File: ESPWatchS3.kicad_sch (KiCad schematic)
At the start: 137 parts, among them J1 USB, J2 OLED, J3 UART0, Q1 DMN2050LFDB, SW1 Reset, SW2 Boot, SW3 User 1, SW4 User 2, SW5 User 3, SW6 User 4, U1 ESP32-S3R8, U10 BD48KxxG, U11 NJG1143UA2-TE1, U2 EVA-M8Q-0, U3 BME280, U4 TPS631000DRLR, U5 AP3012, U6 BQ298012, U7 BQ27441-G1A, U8 BQ24075RGTR, U9 IS25LP128F-JKLE, Y1 40MHz, Y2 32.768kHz, Y3 32.768kHz

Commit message: PCB Work
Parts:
- removed C4: 0.1u, Capacitor_SMD:C_0402_1005Metric, symbol Device:C_Small
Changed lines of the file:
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@@
     (stroke (width 0) (type default))
   )
-  (wire (pts (xy 33.655 106.045) (xy 33.655 108.585))
-    (stroke (width 0) (type default))
-  )
   (wire (pts (xy 51.435 61.595) (xy 51.435 60.325))
     (stroke (width 0) (type default))
@@
     (stroke (width 0) (type default))
   )
-  (wire (pts (xy 26.035 98.425) (xy 33.655 98.425))
-    (stroke (width 0) (type default))
-  )
   (wire (pts (xy 132.715 47.625) (xy 142.24 47.625))
     (stroke (width 0) (type default))
@@
     (stroke (width 0) (type default))
   )
-  (wire (pts (xy 33.655 98.425) (xy 33.655 100.965))
-    (stroke (width 0) (type default))
-  )
   (wire (pts (xy 158.75 186.055) (xy 156.21 186.055))
     (stroke (width 0) (type default))
@@
     )
   )
-  (symbol (lib_id "Device:C_Small") (at 33.655 103.505 0) (unit 1)
-    (in_bom yes) (on_board yes) (dnp no)
-    (property "Reference" "C4" (at 33.655 101.6 0)
-      (effects (font (size 1.27 1.27)) (justify left))
-    )
-    (property "Value" "0.1u" (at 33.655 106.045 0)
-      (effects (font (size 1.27 1.27)) (justify left))
-    )
-    (property "Footprint" "Capacitor_SMD:C_0402_1005Metric" (at 33.655 103.505 0)
-      (effects (font (size 1.27 1.27)) hide)
-    )
-    (property "Datasheet" "~" (at 33.655 103.505 0)
-      (effects (font (size 1.27 1.27)) hide)
-    )
-    (pin "1")
-    (pin "2")
-    (instances
-      (project "ESPWatchS3"
-        (path "/bf5b2c41-bb33-4360-ba29-22d569e03292"
-          (reference "C4") (unit 1)
-        )
-      )
-    )
-  )
   (symbol (lib_id "power:GND") (at 104.775 159.385 0) (unit 1)
     (in_bom yes) (on_board yes) (dnp no) (fields_autoplaced)
@@
         )
       )
-    )
-  )
-  (symbol (lib_id "power:GND") (at 33.655 108.585 0) (unit 1)
-    (in_bom yes) (on_board yes) (dnp no) (fields_autoplaced)
-    (property "Reference" "#PWR024" (at 33.655 114.935 0)
-      (effects (font (size 1.27 1.27)) hide)
-    )
-    (property "Value" "GND" (at 33.655 113.665 0)
-      (effects (font (size 1.27 1.27)))
-    )
-    (property "Footprint" "" (at 33.655 108.585 0)
-      (effects (font (size 1.27 1.27)) hide)
-    )
-    (property "Datasheet" "" (at 33.655 108.585 0)
-      (effects (font (size 1.27 1.27)) hide)
-    )
-    (pin "1")
-    (instances
-      (project "ESPWatchS3"
-        (path "/bf5b2c41-bb33-4360-ba29-22d569e03292"
-          (reference "#PWR024") (unit 1)
-        )
-      )

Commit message: More changes
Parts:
- removed C27: 1u, Capacitor_SMD:C_0603_1608Metric, symbol Device:C_Small
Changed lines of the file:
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@@
   (junction (at 186.69 29.845) (diameter 0) (color 0 0 0 0)
   )
-  (junction (at 368.935 95.25) (diameter 0) (color 0 0 0 0)
-  )
   (junction (at 132.08 186.69) (diameter 0) (color 0 0 0 0)
   )
@@
     (stroke (width 0) (type default))
   )
-  (wire (pts (xy 368.935 104.775) (xy 368.935 113.03))
-    (stroke (width 0) (type default))
-  )
   (wire (pts (xy 34.29 215.265) (xy 29.845 215.265))
     (stroke (width 0) (type default))
@@
     (stroke (width 0) (type default))
   )
-  (wire (pts (xy 368.935 99.695) (xy 368.935 95.25))
-    (stroke (width 0) (type default))
-  )
   (wire (pts (xy 225.425 127.635) (xy 229.87 127.635))
     (stroke (width 0) (type default))
@@
     )
   )
-  (symbol (lib_id "power:GND") (at 368.935 113.03 0) (unit 1)
-    (in_bom yes) (on_board yes) (dnp no) (fields_autoplaced)
-    (property "Reference" "#PWR080" (at 368.935 119.38 0)
-      (effects (font (size 1.27 1.27)) hide)
-    )
-    (property "Value" "GND" (at 368.935 118.11 0)
-      (effects (font (size 1.27 1.27)))
-    )
-    (property "Footprint" "" (at 368.935 113.03 0)
-      (effects (font (size 1.27 1.27)) hide)
-    )
-    (property "Datasheet" "" (at 368.935 113.03 0)
-      (effects (font (size 1.27 1.27)) hide)
-    )
-    (pin "1")
-    (instances
-      (project "ESPWatchS3"
-        (path "/bf5b2c41-bb33-4360-ba29-22d569e03292"
-          (reference "#PWR080") (unit 1)
-        )
-      )
-    )
-  )
   (symbol (lib_id "Device:C_Small") (at 39.37 36.195 0) (unit 1)
     (in_bom yes) (on_board yes) (dnp no) (fields_autoplaced)
@@
         )
       )
-    )
-  )
-  (symbol (lib_id "Device:C_Small") (at 368.935 102.235 0) (mirror y) (unit 1)
-    (in_bom yes) (on_board yes) (dnp no)
-    (property "Reference" "C27" (at 374.015 100.33 0)
-      (effects (font (size 1.27 1.27)) (justify left))
-    )
-    (property "Value" "1u" (at 374.015 102.235 0)
-      (effects (font (size 1.27 1.27)) (justify left))
-    )
-    (property "Footprint" "Capacitor_SMD:C_0603_1608Metric" (at 368.935 102.235 0)
-      (effects (font (size 1.27 1.27)) hide)
-    )
-    (property "Datasheet" "~" (at 368.935 102.235 0)
-      (effects (font (size 1.27 1.27)) hide)
-    )
-    (pin "1")
-    (pin "2")
-    (instances
-      (project "ESPWatchS3"
-        (path "/bf5b2c41-bb33-4360-ba29-22d569e03292"
-          (reference "C27") (unit 1)
-        )
-      )

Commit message: More PCB Work
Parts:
- removed C11, C15, C16: 0.1u, Capacitor_SMD:C_0402_1005Metric, symbol Device:C_Small
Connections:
- net OLED_RES is gone; now on net OLED_RST: J2.11 (Pin_11)

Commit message: More PCB work
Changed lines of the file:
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@@
-    (stroke (width 0) (type default))
-  )
-  (wire (pts (xy 132.08 197.485) (xy 132.08 186.69))
     (stroke (width 0) (type default))
   )
@@
     (stroke (width 0) (type default))
   )
+  (wire (pts (xy 132.08 186.69) (xy 132.08 197.485))
+    (stroke (width 0) (type default))
+  )

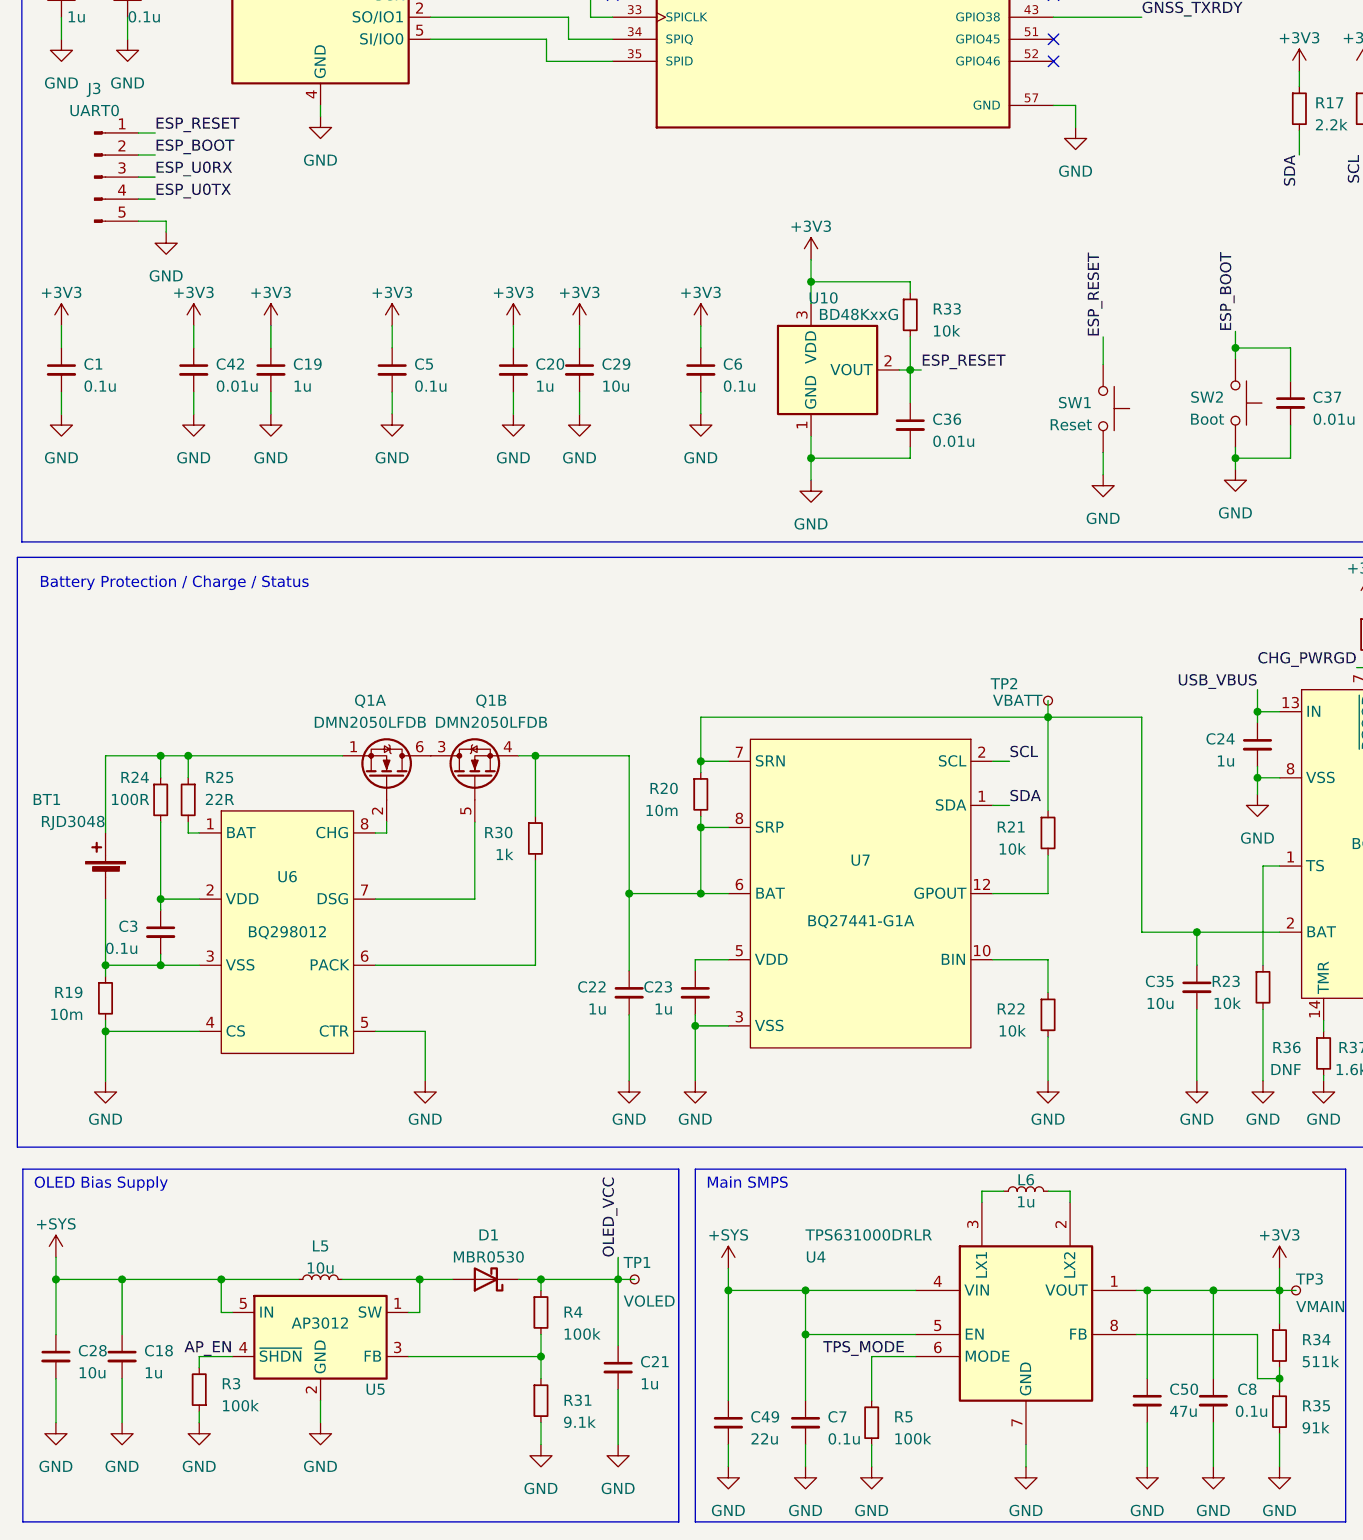
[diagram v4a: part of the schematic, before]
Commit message: Almost done PCB routing
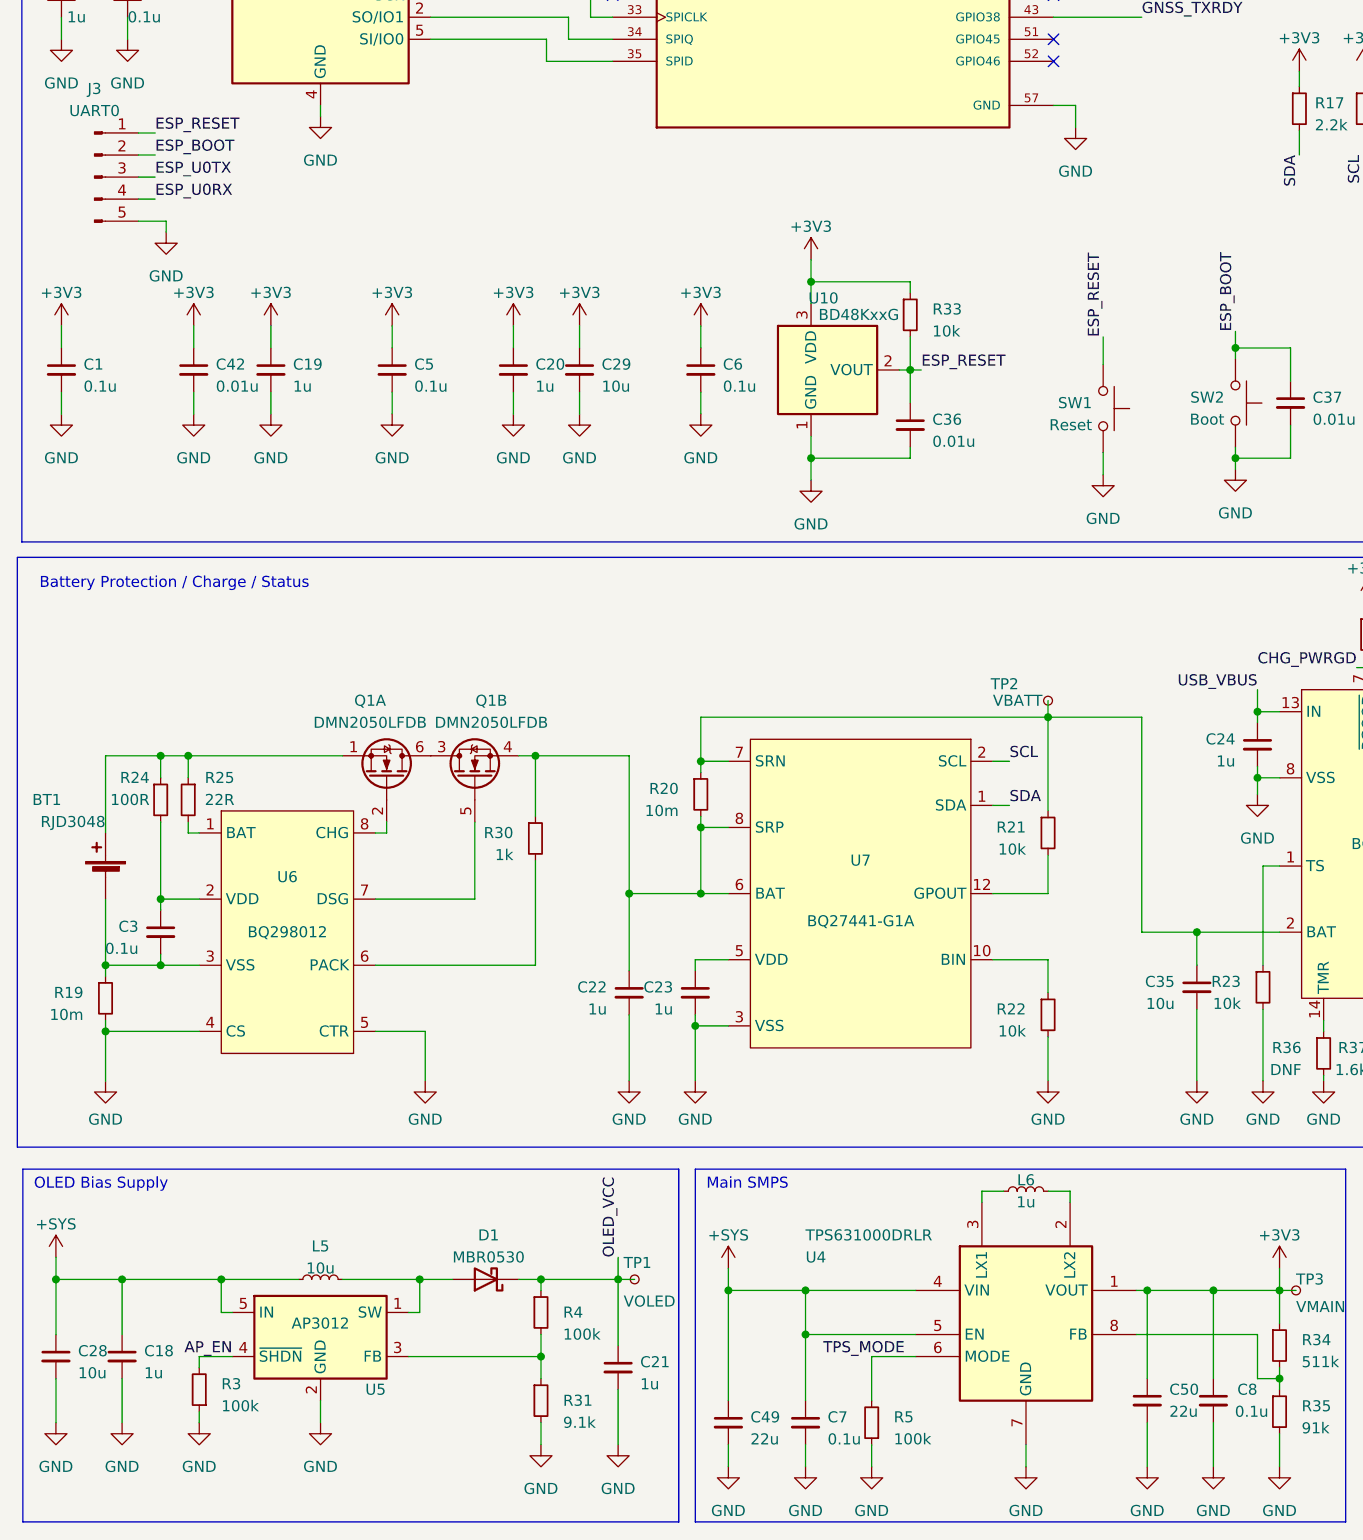
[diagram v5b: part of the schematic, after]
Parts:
- C50: value 47u -> 22u
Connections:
- net ESP_U0RX: now also J3.4 (Pin_4); no longer J3.3 (Pin_3)
- net ESP_U0TX: now also J3.3 (Pin_3); no longer J3.4 (Pin_4)
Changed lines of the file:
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@@
     (effects (font (size 1.27 1.27)) (justify left bottom))
   )
-  (label "ESP_U0TX" (at 29.21 127 0) (fields_autoplaced)
+  (label "ESP_U0TX" (at 29.21 124.46 0) (fields_autoplaced)
     (effects (font (size 1.27 1.27)) (justify left bottom))
   )
@@
     (effects (font (size 1.27 1.27)) (justify right bottom))
   )
-  (label "ESP_U0RX" (at 29.21 124.46 0) (fields_autoplaced)
+  (label "ESP_U0RX" (at 29.21 127 0) (fields_autoplaced)
     (effects (font (size 1.27 1.27)) (justify left bottom))
   )
@@
       (effects (font (size 1.27 1.27)) (justify right))
     )
-    (property "Value" "47u" (at 146.05 266.7 0)
+    (property "Value" "22u" (at 146.05 266.7 0)
       (effects (font (size 1.27 1.27)) (justify right))
     )
